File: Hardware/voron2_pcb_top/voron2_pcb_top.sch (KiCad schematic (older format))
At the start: 19 parts, among them J1 bme280, J10 y_limit, J11 b_motor, J12 a_motor, J13 hotend_fan, J14 x_limit, J15 Conn_01x03, J2 Conn_01x04, J3 probe, J4 extruder, J5 Conn_02x06_Top_Bottom, J6 adxl345, J7 Conn_02x12_Top_Bottom, J8 thermistor, J9 part_fan

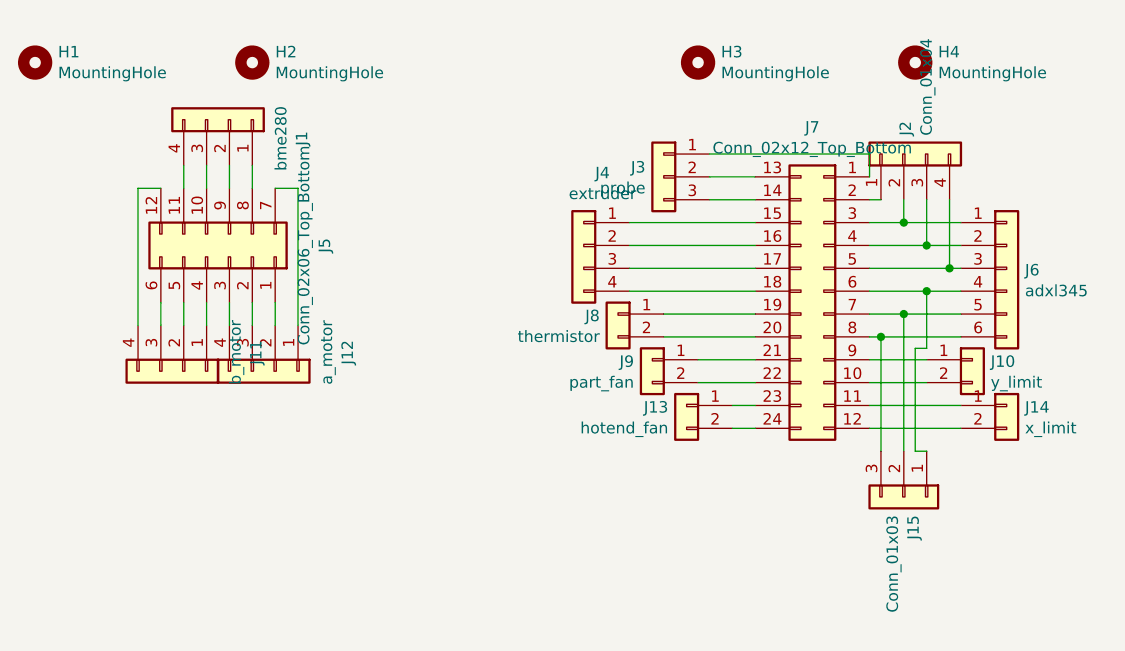
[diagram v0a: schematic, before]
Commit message: Added BAT85 diode to top breakoutboard in top only option.
Added rendered image of top option.
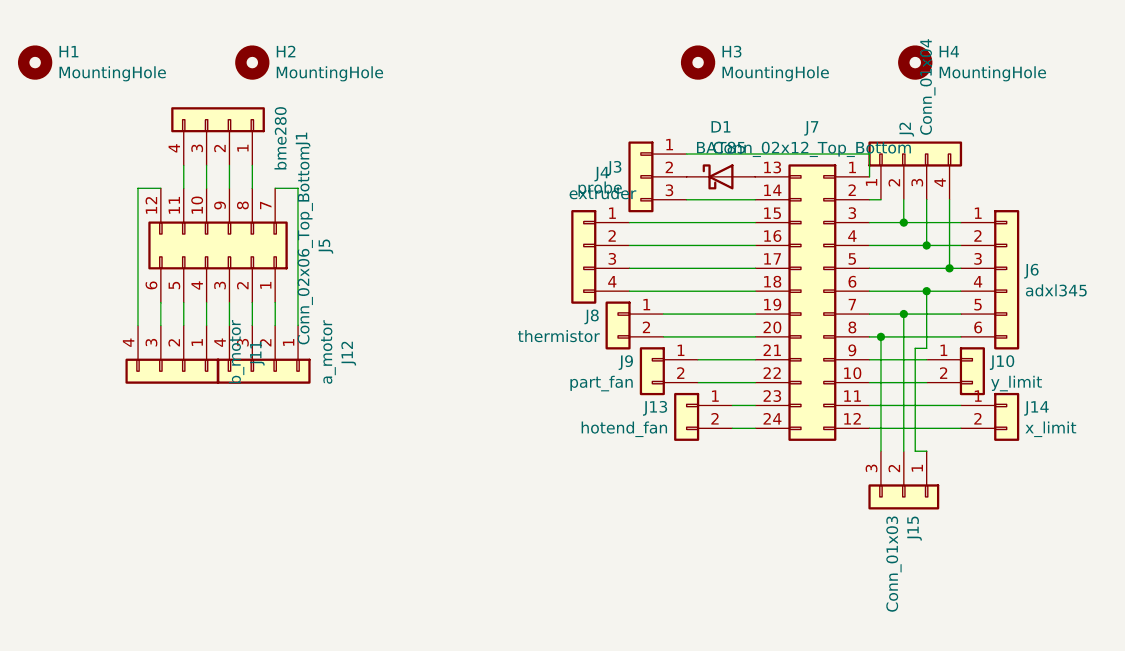
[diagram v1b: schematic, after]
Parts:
- added D1: BAT85, Diode_THT:D_DO-35_SOD27_P7.62mm_Horizontal, symbol Diode:BAT85
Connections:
- net at J7.13 (Pin_13): now also D1.2 (A); no longer J3.2 (Pin_2)
- new net: D1.1 (K), J3.2 (Pin_2)
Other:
- moved on the sheet: J3
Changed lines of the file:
@@
 L Connector_Generic:Conn_01x03 J3
 U 1 1 6033E012
-P 3800 1450
-F 0 "J3" H 3880 1492 50  0000 L CNN
-F 1 "probe" H 3880 1401 50  0000 L CNN
-F 2 "Connector_JST:JST_XH_B3B-XH-A_1x03_P2.50mm_Vertical" H 3800 1450 50  0001 C CNN
-F 3 "~" H 3800 1450 50  0001 C CNN
-	1    3800 1450
+P 3700 1450
+F 0 "J3" H 3780 1492 50  0000 L CNN
+F 1 "probe" H 3780 1401 50  0000 L CNN
+F 2 "Connector_JST:JST_XH_B3B-XH-A_1x03_P2.50mm_Vertical" H 3700 1450 50  0001 C CNN
+F 3 "~" H 3700 1450 50  0001 C CNN
+	1    3700 1450
 	-1   0    0    -1
 $EndComp
@@
 Wire Wire Line
 	4200 1950 3650 1950
-Wire Wire Line
-	4000 1550 4200 1550
-Wire Wire Line
-	4200 1450 4000 1450
-Wire Wire Line
-	4000 1350 4700 1350
 Wire Wire Line
 	4700 1350 4700 1450
@@
 Wire Wire Line
 	2000 1500 2000 1400
+$Comp
+L Diode:BAT85 D1
+U 1 1 60402B54
+P 4050 1450
+F 0 "D1" H 4050 1667 50  0000 C CNN
+F 1 "BAT85" H 4050 1576 50  0000 C CNN
+F 2 "Diode_THT:D_DO-35_SOD27_P7.62mm_Horizontal" H 4050 1275 50  0001 C CNN
+F 3 "https://assets.nexperia.com/documents/data-sheet/BAT85.pdf" H 4050 1450 50  0001 C CNN
+	1    4050 1450
+	1    0    0    -1
+$EndComp
+Wire Wire Line
+	3900 1550 4200 1550
+Wire Wire Line
+	3900 1350 4700 1350
 $EndSCHEMATC

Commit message: Separated top in top and back for easier production.
Added renders of top and back PCBs.
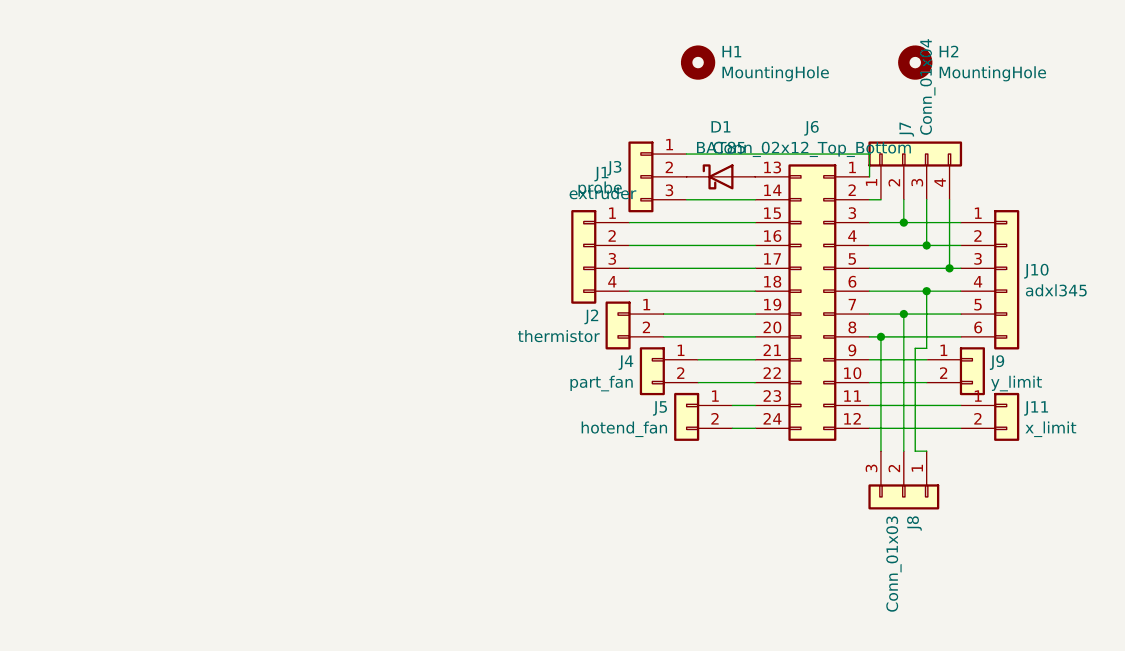
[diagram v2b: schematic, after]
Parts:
- removed H1, H2: MountingHole, MountingHole:MountingHole_3.2mm_M3, symbol Mechanical:MountingHole
- removed J1: bme280, Connector_JST:JST_XH_B4B-XH-A_1x04_P2.50mm_Vertical, symbol Connector_Generic:Conn_01x04
- removed J11: b_motor, Connector_JST:JST_XH_B4B-XH-A_1x04_P2.50mm_Vertical, symbol Connector_Generic:Conn_01x04
- removed J12: a_motor, Connector_JST:JST_XH_B4B-XH-A_1x04_P2.50mm_Vertical, symbol Connector_Generic:Conn_01x04
- removed J5: Conn_02x06_Top_Bottom, Connector_Molex:Molex_Micro-Fit_3.0_43045-1212_2x06_P3.00mm_Vertical, symbol Connector_Generic:Conn_02x06_Top_Bottom
- renumbered H3 to H1, H4 to H2, J4 to J1, J6 to J10, J14 to J11, J8 to J2, J9 to J4, J13 to J5, J7 to J6, J2 to J7, J15 to J8, J10 to J9
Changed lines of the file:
@@
 $Comp
 L Mechanical:MountingHole H1
-U 1 1 60327C40
-P 1050 950
-F 0 "H1" H 1150 996 50  0000 L CNN
-F 1 "MountingHole" H 1150 905 50  0000 L CNN
-F 2 "MountingHole:MountingHole_3.2mm_M3" H 1050 950 50  0001 C CNN
-F 3 "~" H 1050 950 50  0001 C CNN
-	1    1050 950
-	1    0    0    -1
-$EndComp
-$Comp
-L Mechanical:MountingHole H2
-U 1 1 60329100
-P 2000 950
-F 0 "H2" H 2100 996 50  0000 L CNN
-F 1 "MountingHole" H 2100 905 50  0000 L CNN
-F 2 "MountingHole:MountingHole_3.2mm_M3" H 2000 950 50  0001 C CNN
-F 3 "~" H 2000 950 50  0001 C CNN
-	1    2000 950
-	1    0    0    -1
-$EndComp
-$Comp
-L Mechanical:MountingHole H3
 U 1 1 60329240
 P 3950 950
-F 0 "H3" H 4050 996 50  0000 L CNN
+F 0 "H1" H 4050 996 50  0000 L CNN
 F 1 "MountingHole" H 4050 905 50  0000 L CNN
 F 2 "MountingHole:MountingHole_3.2mm_M3" H 3950 950 50  0001 C CNN
@@
 $EndComp
 $Comp
-L Mechanical:MountingHole H4
+L Mechanical:MountingHole H2
 U 1 1 60329885
 P 4900 950
-F 0 "H4" H 5000 996 50  0000 L CNN
+F 0 "H2" H 5000 996 50  0000 L CNN
 F 1 "MountingHole" H 5000 905 50  0000 L CNN
 F 2 "MountingHole:MountingHole_3.2mm_M3" H 4900 950 50  0001 C CNN
@@
 $EndComp
 $Comp
-L Connector_Generic:Conn_02x06_Top_Bottom J5
-U 1 1 6032AC6E
-P 1900 1800
-F 0 "J5" H 1950 2217 50  0000 C CNN
-F 1 "Conn_02x06_Top_Bottom" H 1950 2126 50  0000 C CNN
-F 2 "Connector_Molex:Molex_Micro-Fit_3.0_43045-1212_2x06_P3.00mm_Vertical" H 1900 1800 50  0001 C CNN
-F 3 "~" H 1900 1800 50  0001 C CNN
-	1    1900 1800
-	0    1    -1   0
-$EndComp
-$Comp
-L Connector_Generic:Conn_02x12_Top_Bottom J7
+L Connector_Generic:Conn_02x12_Top_Bottom J6
 U 1 1 6032E07F
 P 4500 1950
-F 0 "J7" H 4550 2667 50  0000 C CNN
+F 0 "J6" H 4550 2667 50  0000 C CNN
 F 1 "Conn_02x12_Top_Bottom" H 4550 2576 50  0000 C CNN
 F 2 "Connector_Molex:Molex_Micro-Fit_3.0_43045-2412_2x12_P3.00mm_Vertical" H 4500 1950 50  0001 C CNN
@@
 $Comp
 L Connector_Generic:Conn_01x04 J1
-U 1 1 603375A8
-P 1900 1200
-F 0 "J1" H 1818 1517 50  0000 C CNN
-F 1 "bme280" H 1818 1426 50  0000 C CNN
-F 2 "Connector_JST:JST_XH_B4B-XH-A_1x04_P2.50mm_Vertical" H 1900 1200 50  0001 C CNN
-F 3 "~" H 1900 1200 50  0001 C CNN
-	1    1900 1200
-	0    1    -1   0
-$EndComp
-$Comp
-L Connector_Generic:Conn_01x04 J11
-U 1 1 6033945F
-P 1700 2300
-F 0 "J11" H 1618 2617 50  0000 C CNN
-F 1 "b_motor" H 1618 2526 50  0000 C CNN
-F 2 "Connector_JST:JST_XH_B4B-XH-A_1x04_P2.50mm_Vertical" H 1700 2300 50  0001 C CNN
-F 3 "~" H 1700 2300 50  0001 C CNN
-	1    1700 2300
-	0    1    1    0
-$EndComp
-$Comp
-L Connector_Generic:Conn_01x04 J12
-U 1 1 603394FE
-P 2100 2300
-F 0 "J12" H 2018 2617 50  0000 C CNN
-F 1 "a_motor" H 2018 2526 50  0000 C CNN
-F 2 "Connector_JST:JST_XH_B4B-XH-A_1x04_P2.50mm_Vertical" H 2100 2300 50  0001 C CNN
-F 3 "~" H 2100 2300 50  0001 C CNN
-	1    2100 2300
-	0    1    1    0
-$EndComp
-$Comp
-L Connector_Generic:Conn_01x04 J4
 U 1 1 6033A4F3
 P 3450 1750
-F 0 "J4" H 3368 2067 50  0000 C CNN
+F 0 "J1" H 3368 2067 50  0000 C CNN
 F 1 "extruder" H 3368 1976 50  0000 C CNN
 F 2 "Connector_JST:JST_XH_B4B-XH-A_1x04_P2.50mm_Vertical" H 3450 1750 50  0001 C CNN
@@
 $EndComp
 $Comp
-L Connector_Generic:Conn_01x02 J10
+L Connector_Generic:Conn_01x02 J9
 U 1 1 6033AA39
 P 5150 2250
-F 0 "J10" H 5230 2242 50  0000 L CNN
+F 0 "J9" H 5230 2242 50  0000 L CNN
 F 1 "y_limit" H 5230 2151 50  0000 L CNN
 F 2 "Connector_JST:JST_XH_B2B-XH-A_1x02_P2.50mm_Vertical" H 5150 2250 50  0001 C CNN
@@
 $EndComp
 $Comp
-L Connector_Generic:Conn_01x02 J14
+L Connector_Generic:Conn_01x02 J11
 U 1 1 6033C38B
 P 5300 2450
-F 0 "J14" H 5380 2442 50  0000 L CNN
+F 0 "J11" H 5380 2442 50  0000 L CNN
 F 1 "x_limit" H 5380 2351 50  0000 L CNN
 F 2 "Connector_JST:JST_XH_B2B-XH-A_1x02_P2.50mm_Vertical" H 5300 2450 50  0001 C CNN
@@
 $EndComp
 $Comp
-L Connector_Generic:Conn_01x02 J8
+L Connector_Generic:Conn_01x02 J2
 U 1 1 6033C577
 P 3600 2050
-F 0 "J8" H 3680 2042 50  0000 L CNN
+F 0 "J2" H 3680 2042 50  0000 L CNN
 F 1 "thermistor" H 3680 1951 50  0000 L CNN
 F 2 "Connector_JST:JST_XH_B2B-XH-A_1x02_P2.50mm_Vertical" H 3600 2050 50  0001 C CNN
@@
 $EndComp
 $Comp
-L Connector_Generic:Conn_01x02 J13
+L Connector_Generic:Conn_01x02 J5
 U 1 1 6033CC60
 P 3900 2450
-F 0 "J13" H 3980 2442 50  0000 L CNN
+F 0 "J5" H 3980 2442 50  0000 L CNN
 F 1 "hotend_fan" H 3980 2351 50  0000 L CNN
 F 2 "Connector_JST:JST_XH_B2B-XH-A_1x02_P2.50mm_Vertical" H 3900 2450 50  0001 C CNN
@@
 $EndComp
 $Comp
-L Connector_Generic:Conn_01x06 J6
+L Connector_Generic:Conn_01x06 J10
 U 1 1 6033F5F6
 P 5300 1850
-F 0 "J6" H 5380 1842 50  0000 L CNN
+F 0 "J10" H 5380 1842 50  0000 L CNN
 F 1 "adxl345" H 5380 1751 50  0000 L CNN
 F 2 "Connector_JST:JST_XH_B6B-XH-A_1x06_P2.50mm_Vertical" H 5300 1850 50  0001 C CNN
@@
 	4950 2350 4700 2350
 $Comp
-L Connector_Generic:Conn_01x02 J9
+L Connector_Generic:Conn_01x02 J4
 U 1 1 6033C920
 P 3750 2250
-F 0 "J9" H 3830 2242 50  0000 L CNN
+F 0 "J4" H 3830 2242 50  0000 L CNN
 F 1 "part_fan" H 3830 2151 50  0000 L CNN
 F 2 "Connector_JST:JST_XH_B2B-XH-A_1x02_P2.50mm_Vertical" H 3750 2250 50  0001 C CNN
@@
 	4100 2550 4200 2550
 $Comp
-L Connector_Generic:Conn_01x03 J15
+L Connector_Generic:Conn_01x03 J8
 U 1 1 603E406F
 P 4850 2850
-F 0 "J15" H 4930 2892 50  0000 L CNN
+F 0 "J8" H 4930 2892 50  0000 L CNN
 F 1 "Conn_01x03" H 4930 2801 50  0000 L CNN
 F 2 "Connector_PinHeader_2.54mm:PinHeader_1x03_P2.54mm_Vertical" H 4850 2850 50  0001 C CNN
@@
 $EndComp
 $Comp
-L Connector_Generic:Conn_01x04 J2
+L Connector_Generic:Conn_01x04 J7
 U 1 1 603E4593
 P 4850 1350
-F 0 "J2" H 4930 1342 50  0000 L CNN
+F 0 "J7" H 4930 1342 50  0000 L CNN
 F 1 "Conn_01x04" H 4930 1251 50  0000 L CNN
 F 2 "Connector_PinHeader_2.54mm:PinHeader_1x04_P2.54mm_Vertical" H 4850 1350 50  0001 C CNN
@@
 Wire Wire Line
 	4950 1950 5100 1950
-Wire Wire Line
-	1600 2100 1600 2000
-Wire Wire Line
-	1700 2000 1700 2100
-Wire Wire Line
-	1800 2100 1800 2000
-Wire Wire Line
-	1900 2000 1900 2100
-Wire Wire Line
-	2000 2100 2000 2000
-Wire Wire Line
-	2100 2000 2100 2100
-Wire Wire Line
-	2200 2100 2200 1500
-Wire Wire Line
-	2200 1500 2100 1500
-Wire Wire Line
-	1600 1500 1500 1500
-Wire Wire Line
-	1500 1500 1500 2100
-Wire Wire Line
-	1700 1400 1700 1500
-Wire Wire Line
-	1800 1500 1800 1400
-Wire Wire Line
-	1900 1400 1900 1500
-Wire Wire Line
-	2000 1500 2000 1400
 $Comp
 L Diode:BAT85 D1
